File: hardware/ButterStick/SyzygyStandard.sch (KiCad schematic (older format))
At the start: 9 parts, among them J1 SYZYGY-STD, U2 DAC081C081CIMK, U7 TPS73101DBV

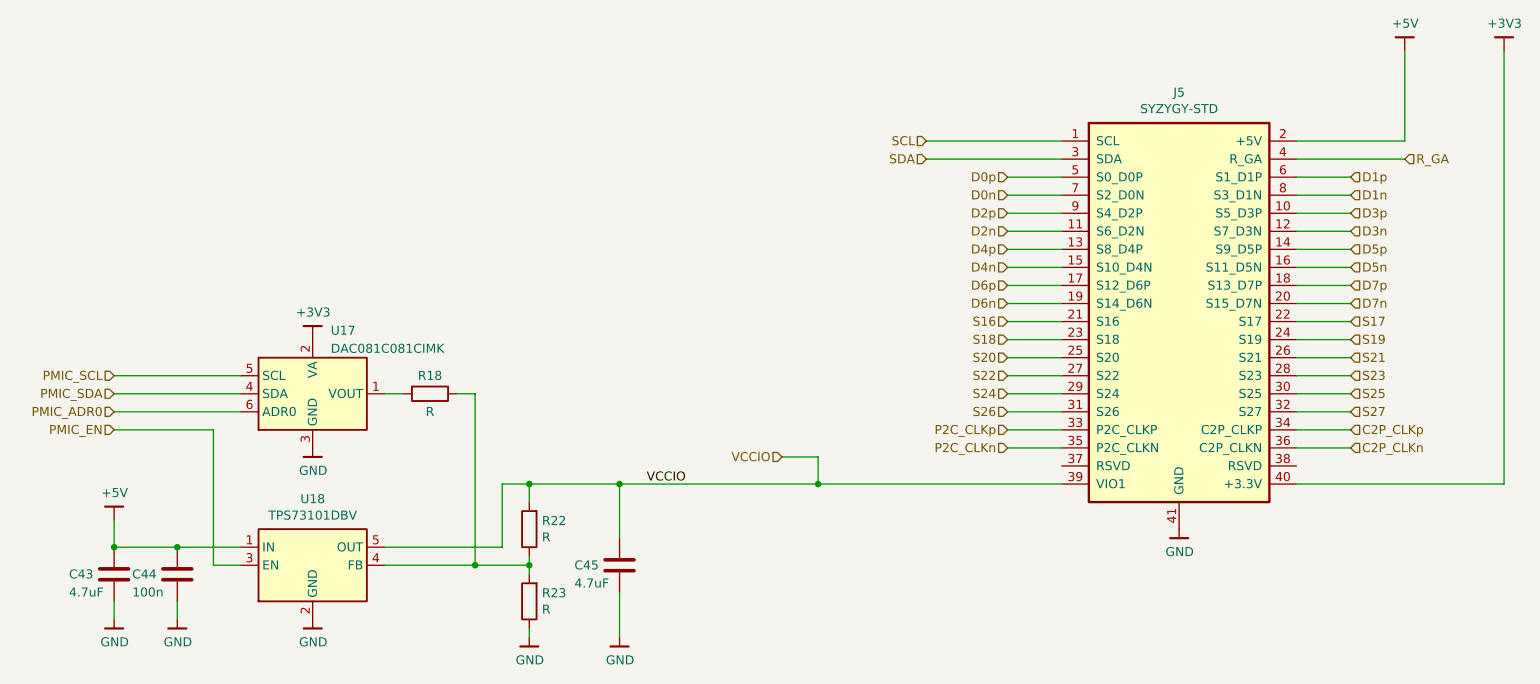
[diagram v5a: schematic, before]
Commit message: Finalised part values update BOM values to reflect. Swapped layers 4/5 due to stackup changes
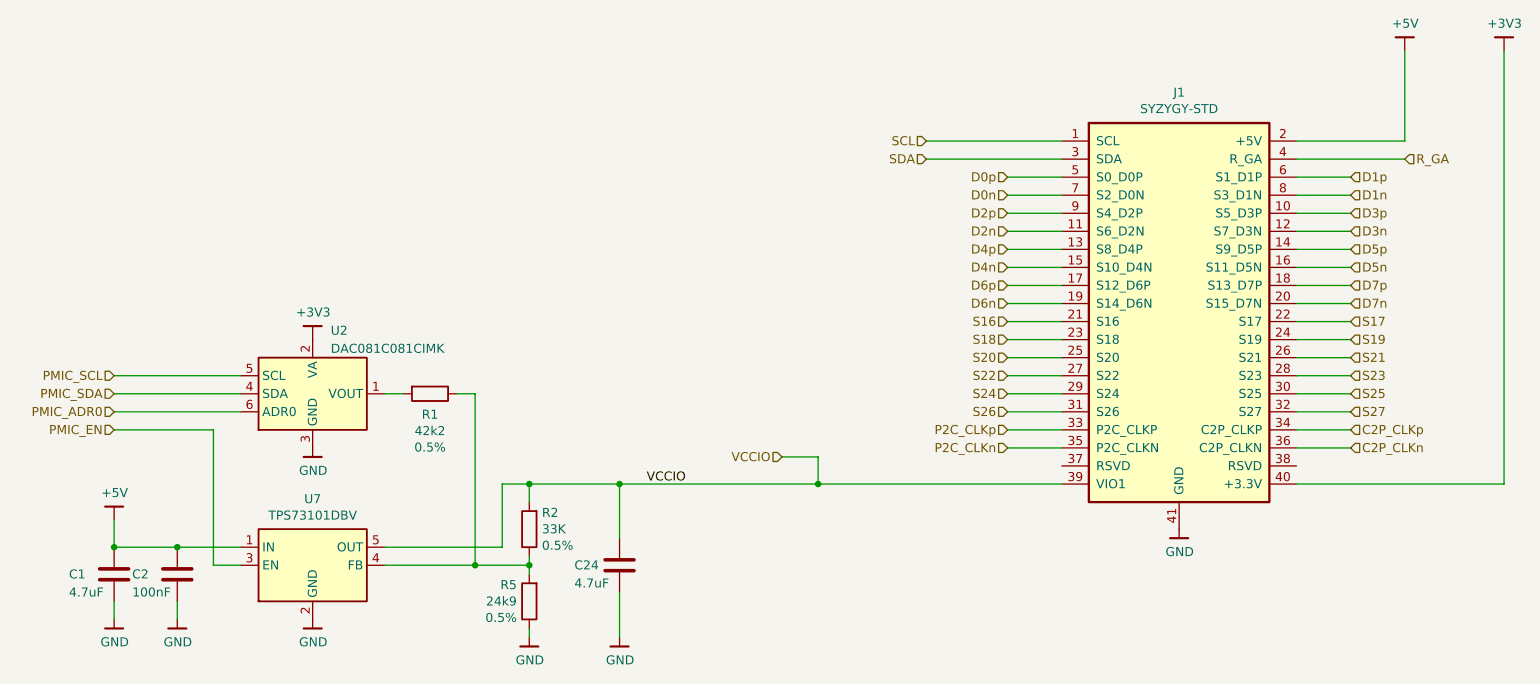
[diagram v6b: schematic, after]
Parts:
- C1, C24: Mfg (none) -> Samsung Electro-Mechanics; PN (none) -> CL10A475KP8NNNC
- C2: value 100n -> 100nF; Mfg (none) -> Samsung Electro-Mechanics; PN (none) -> CL05B104KP5NNNC
- J1: Mfg (none) -> Samtec Inc.; PN (none) -> QSE-020-01-F-D-A
- R1: value R -> 42k2; Mfg (none) -> Stackpole Electronics Inc; PN (none) -> RNCF0402DTE42K2; Tol (none) -> 0.5%
- R2: value R -> 33K; Mfg (none) -> Stackpole Electronics Inc; PN (none) -> RNCF0402DTE33K0; Tol (none) -> 0.5%
- R5: value R -> 24k9; Mfg (none) -> Stackpole Electronics Inc; PN (none) -> RNCF0402DTE24K9; Tol (none) -> 0.5%
- U2: Mfg (none) -> Texas Instruments; PN (none) -> DAC081C081CIMK/NOPB
- U7: Mfg (none) -> Texas Instruments; PN (none) -> TPS73101DBVR
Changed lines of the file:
@@
 EESchema Schematic File Version 4
 LIBS:ButterStick-cache
-EELAYER 26 0
+EELAYER 29 0
 EELAYER END
 $Descr A4 11693 8268
 encoding utf-8
-Sheet 8 13
-Title ""
-Date ""
-Rev ""
-Comp ""
+Sheet 6 13
+Title "ButterStick"
+Date "2019-03-19"
+Rev "r0_1"
+Comp "GsD"
 Comment1 ""
 Comment2 ""
@@
 AR Path="/5C80F19D/5C8A3B67/5C813052" Ref="J3"  Part="1"
 AR Path="/5C80F1A0/5C8EBB21/5C813052" Ref="J5"  Part="1"
-F 0 "J5" H 7850 4819 50  0000 C CNN
+F 0 "J1" H 7850 4819 50  0000 C CNN
 F 1 "SYZYGY-STD" H 7850 4728 50  0000 C CNN
 F 2 "gkl_conn:SYZYGY_standard_carrier" H 7850 4700 50  0001 C CNN
 F 3 "" H 7850 4700 50  0001 C CNN
+F 4 "Samtec Inc." H 0   0   50  0001 C CNN "Mfg"
+F 5 "QSE-020-01-F-D-A" H 0   0   50  0001 C CNN "PN"
 	1    7850 3700
 	1    0    0    -1
@@
 AR Path="/5C80F19D/5C8A3B67/5C939EEE" Ref="U16"  Part="1"
 AR Path="/5C80F1A0/5C8EBB21/5C939EEE" Ref="U18"  Part="1"
-F 0 "U18" H 3050 5567 50  0000 C CNN
+F 0 "U7" H 3050 5567 50  0000 C CNN
 F 1 "TPS73101DBV" H 3050 5476 50  0000 C CNN
 F 2 "Package_TO_SOT_SMD:SOT-23-5" H 3050 5525 50  0001 C CIN
 F 3 "http://www.ti.com/lit/ds/symlink/tps731.pdf" H 3050 5150 50  0001 C CNN
+F 4 "Texas Instruments" H 0   0   50  0001 C CNN "Mfg"
+F 5 "TPS73101DBVR" H 0   0   50  0001 C CNN "PN"
 	1    3050 5200
 	1    0    0    -1
@@
 AR Path="/5C80F19D/5C8A3B67/5C939EF5" Ref="U12"  Part="1"
 AR Path="/5C80F1A0/5C8EBB21/5C939EF5" Ref="U17"  Part="1"
-F 0 "U17" H 3150 4600 50  0000 L CNN
+F 0 "U2" H 3150 4600 50  0000 L CNN
 F 1 "DAC081C081CIMK" H 3150 4500 50  0000 L CNN
 F 2 "Package_TO_SOT_SMD:SOT-23-6" H 3700 4000 50  0001 C CNN
 F 3 "http://www.ti.com/lit/ds/symlink/dac081c081.pdf" H 3050 4250 50  0001 C CNN
+F 4 "Texas Instruments" H 0   0   50  0001 C CNN "Mfg"
+F 5 "DAC081C081CIMK/NOPB" H 0   0   50  0001 C CNN "PN"
 	1    3050 4250
 	1    0    0    -1
@@
 AR Path="/5C80F19D/5C8A3B67/5C9A2E64" Ref="#PWR0140"  Part="1"
 AR Path="/5C80F1A0/5C8EBB21/5C9A2E64" Ref="#PWR0183"  Part="1"
-F 0 "#PWR0183" H 3050 4300 50  0001 C CNN
+F 0 "#PWR0125" H 3050 4300 50  0001 C CNN
 F 1 "GND" H 3053 4424 50  0000 C CNN
 F 2 "" H 2950 4200 50  0001 C CNN
@@
 AR Path="/5C80F19D/5C8A3B67/5C939F02" Ref="#PWR0173"  Part="1"
 AR Path="/5C80F1A0/5C8EBB21/5C939F02" Ref="#PWR0184"  Part="1"
-F 0 "#PWR0184" H 3050 5250 50  0001 C CNN
+F 0 "#PWR0130" H 3050 5250 50  0001 C CNN
 F 1 "GND" H 3053 5374 50  0000 C CNN
 F 2 "" H 2950 5150 50  0001 C CNN
@@
 AR Path="/5C80F19D/5C8A3B67/5C9A2E66" Ref="#PWR0174"  Part="1"
 AR Path="/5C80F1A0/5C8EBB21/5C9A2E66" Ref="#PWR0185"  Part="1"
-F 0 "#PWR0185" H 3050 3800 50  0001 C CNN
+F 0 "#PWR0131" H 3050 3800 50  0001 C CNN
 F 1 "+3V3" H 3053 4101 50  0000 C CNN
 F 2 "" H 3050 3950 50  0001 C CNN
@@
 AR Path="/5C80F19D/5C8A3B67/5C939F0E" Ref="#PWR0175"  Part="1"
 AR Path="/5C80F1A0/5C8EBB21/5C939F0E" Ref="#PWR0186"  Part="1"
-F 0 "#PWR0186" H 1950 4800 50  0001 C CNN
+F 0 "#PWR0132" H 1950 4800 50  0001 C CNN
 F 1 "+5V" H 1953 5101 50  0000 C CNN
 F 2 "" H 1950 4950 50  0001 C CNN
@@
 AR Path="/5C80F19D/5C8A3B67/5C9A2E68" Ref="C38"  Part="1"
 AR Path="/5C80F1A0/5C8EBB21/5C9A2E68" Ref="C43"  Part="1"
-F 0 "C43" H 1700 5250 50  0000 L CNN
+F 0 "C1" H 1700 5250 50  0000 L CNN
 F 1 "4.7uF" H 1700 5150 50  0000 L CNN
 F 2 "pkl_dipol:C_0603" H 1988 5100 50  0001 C CNN
 F 3 "~" H 1950 5250 50  0001 C CNN
+F 4 "Samsung Electro-Mechanics" H 0   0   50  0001 C CNN "Mfg"
+F 5 "CL10A475KP8NNNC" H 0   0   50  0001 C CNN "PN"
 	1    1950 5250
 	1    0    0    -1
@@
 AR Path="/5C80F19D/5C8A3B67/5C939F1D" Ref="C39"  Part="1"
 AR Path="/5C80F1A0/5C8EBB21/5C939F1D" Ref="C44"  Part="1"
-F 0 "C44" H 2050 5250 50  0000 L CNN
-F 1 "100n" H 2050 5150 50  0000 L CNN
+F 0 "C2" H 2050 5250 50  0000 L CNN
+F 1 "100nF" H 2050 5150 50  0000 L CNN
 F 2 "pkl_dipol:C_0402" H 2338 5100 50  0001 C CNN
 F 3 "~" H 2300 5250 50  0001 C CNN
+F 4 "Samsung Electro-Mechanics" H 0   0   50  0001 C CNN "Mfg"
+F 5 "CL05B104KP5NNNC" H 0   0   50  0001 C CNN "PN"
 	1    2300 5250
 	1    0    0    -1
@@
 AR Path="/5C80F19D/5C8A3B67/5C9A2E6A" Ref="R6"  Part="1"
 AR Path="/5C80F1A0/5C8EBB21/5C9A2E6A" Ref="R18"  Part="1"
-F 0 "R18" V 3600 4250 50  0000 C CNN
-F 1 "R" V 3800 4250 50  0000 C CNN
+F 0 "R1" V 3815 4250 50  0000 C CNN
+F 1 "42k2" V 3906 4250 50  0000 C CNN
 F 2 "pkl_dipol:C_0402" V 3630 4250 50  0001 C CNN
 F 3 "~" H 3700 4250 50  0001 C CNN
+F 4 "RNCF0402DTE42K2" H 3700 4250 50  0001 C CNN "PN"
+F 5 "Stackpole Electronics Inc" H 3700 4250 50  0001 C CNN "Mfg"
+F 6 "0.5%" V 3997 4250 50  0000 C CNN "Tol"
 	1    3700 4250
 	0    1    1    0
-$EndComp
-$Comp
-L Device:R R?
-U 1 1 5C939F38
-P 4250 5000
-AR Path="/5BBD18EA/5C939F38" Ref="R?"  Part="1"
-AR Path="/5C80F19A/5C812FEF/5C939F38" Ref="R2"  Part="1"
-AR Path="/5C80F19D/5C8A3B67/5C939F38" Ref="R16"  Part="1"
-AR Path="/5C80F1A0/5C8EBB21/5C939F38" Ref="R22"  Part="1"
-F 0 "R22" H 4180 4954 50  0000 R CNN
-F 1 "R" H 4180 5045 50  0000 R CNN
-F 2 "pkl_dipol:C_0402" V 4180 5000 50  0001 C CNN
-F 3 "~" H 4250 5000 50  0001 C CNN
-	1    4250 5000
-	-1   0    0    1
 $EndComp
 $Comp
@@
 AR Path="/5C80F19D/5C8A3B67/5C939F3F" Ref="R17"  Part="1"
 AR Path="/5C80F1A0/5C8EBB21/5C939F3F" Ref="R23"  Part="1"
-F 0 "R23" H 4180 5354 50  0000 R CNN
-F 1 "R" H 4180 5445 50  0000 R CNN
+F 0 "R5" H 4319 5309 50  0000 L CNN
+F 1 "24k9" H 4319 5400 50  0000 L CNN
 F 2 "pkl_dipol:C_0402" V 4180 5400 50  0001 C CNN
 F 3 "~" H 4250 5400 50  0001 C CNN
+F 4 "RNCF0402DTE24K9" H 4250 5400 50  0001 C CNN "PN"
+F 5 "Stackpole Electronics Inc" H 4250 5400 50  0001 C CNN "Mfg"
+F 6 "0.5%" H 4319 5491 50  0000 L CNN "Tol"
 	1    4250 5400
 	-1   0    0    1
@@
 AR Path="/5C80F19D/5C8A3B67/5C939F46" Ref="C42"  Part="1"
 AR Path="/5C80F1A0/5C8EBB21/5C939F46" Ref="C45"  Part="1"
-F 0 "C45" H 4500 5200 50  0000 L CNN
+F 0 "C24" H 4500 5200 50  0000 L CNN
 F 1 "4.7uF" H 4500 5100 50  0000 L CNN
 F 2 "pkl_dipol:C_0603" H 4788 5050 50  0001 C CNN
 F 3 "~" H 4750 5200 50  0001 C CNN
+F 4 "Samsung Electro-Mechanics" H 0   0   50  0001 C CNN "Mfg"
+F 5 "CL10A475KP8NNNC" H 0   0   50  0001 C CNN "PN"
 	1    4750 5200
 	1    0    0    -1
@@
 AR Path="/5C80F19D/5C8A3B67/5C939F4E" Ref="#PWR0176"  Part="1"
 AR Path="/5C80F1A0/5C8EBB21/5C939F4E" Ref="#PWR0187"  Part="1"
-F 0 "#PWR0187" H 4250 5350 50  0001 C CNN
+F 0 "#PWR0133" H 4250 5350 50  0001 C CNN
 F 1 "GND" H 4253 5474 50  0000 C CNN
 F 2 "" H 4150 5250 50  0001 C CNN
@@
 AR Path="/5C80F19D/5C8A3B67/5C9A2E6F" Ref="#PWR0177"  Part="1"
 AR Path="/5C80F1A0/5C8EBB21/5C9A2E6F" Ref="#PWR0188"  Part="1"
-F 0 "#PWR0188" H 4750 5350 50  0001 C CNN
+F 0 "#PWR0134" H 4750 5350 50  0001 C CNN
 F 1 "GND" H 4753 5474 50  0000 C CNN
 F 2 "" H 4650 5250 50  0001 C CNN
@@
 AR Path="/5C80F19D/5C8A3B67/5C939F6F" Ref="#PWR0178"  Part="1"
 AR Path="/5C80F1A0/5C8EBB21/5C939F6F" Ref="#PWR0189"  Part="1"
-F 0 "#PWR0189" H 2300 5250 50  0001 C CNN
+F 0 "#PWR0135" H 2300 5250 50  0001 C CNN
 F 1 "GND" H 2303 5374 50  0000 C CNN
 F 2 "" H 2200 5150 50  0001 C CNN
@@
 AR Path="/5C80F19D/5C8A3B67/5C939F75" Ref="#PWR0179"  Part="1"
 AR Path="/5C80F1A0/5C8EBB21/5C939F75" Ref="#PWR0190"  Part="1"
-F 0 "#PWR0190" H 1950 5250 50  0001 C CNN
+F 0 "#PWR0137" H 1950 5250 50  0001 C CNN
 F 1 "GND" H 1953 5374 50  0000 C CNN
 F 2 "" H 1850 5150 50  0001 C CNN
@@
 AR Path="/5C80F19D/5C8A3B67/5C946418" Ref="#PWR0181"  Part="1"
 AR Path="/5C80F1A0/5C8EBB21/5C946418" Ref="#PWR0191"  Part="1"
-F 0 "#PWR0191" H 9100 2200 50  0001 C CNN
+F 0 "#PWR0138" H 9100 2200 50  0001 C CNN
 F 1 "+5V" H 9103 2501 50  0000 C CNN
 F 2 "" H 9100 2350 50  0001 C CNN
@@
 AR Path="/5C80F19D/5C8A3B67/5C946494" Ref="#PWR0182"  Part="1"
 AR Path="/5C80F1A0/5C8EBB21/5C946494" Ref="#PWR0211"  Part="1"
-F 0 "#PWR0211" H 9650 2200 50  0001 C CNN
+F 0 "#PWR0139" H 9650 2200 50  0001 C CNN
 F 1 "+3V3" H 9653 2501 50  0000 C CNN
 F 2 "" H 9650 2350 50  0001 C CNN
@@
 AR Path="/5C80F19D/5C8A3B67/5CED2F7B" Ref="#PWR0265"  Part="1"
 AR Path="/5C80F1A0/5C8EBB21/5CED2F7B" Ref="#PWR0266"  Part="1"
-F 0 "#PWR0266" H 7850 4750 50  0001 C CNN
+F 0 "#PWR0264" H 7850 4750 50  0001 C CNN
 F 1 "GND" H 7853 4874 50  0000 C CNN
 F 2 "" H 7750 4650 50  0001 C CNN
@@
 Wire Wire Line
 	1950 4450 2500 4450
+$Comp
+L Device:R R?
+U 1 1 5C939F38
+P 4250 5000
+AR Path="/5BBD18EA/5C939F38" Ref="R?"  Part="1"
+AR Path="/5C80F19A/5C812FEF/5C939F38" Ref="R2"  Part="1"
+AR Path="/5C80F19D/5C8A3B67/5C939F38" Ref="R16"  Part="1"
+AR Path="/5C80F1A0/5C8EBB21/5C939F38" Ref="R22"  Part="1"
+F 0 "R2" H 4180 4909 50  0000 R CNN
+F 1 "33K" H 4180 5000 50  0000 R CNN
+F 2 "pkl_dipol:C_0402" V 4180 5000 50  0001 C CNN
+F 3 "~" H 4250 5000 50  0001 C CNN
+F 4 "RNCF0402DTE33K0" H 4250 5000 50  0001 C CNN "PN"
+F 5 "Stackpole Electronics Inc" H 4250 5000 50  0001 C CNN "Mfg"
+F 6 "0.5%" H 4180 5091 50  0000 R CNN "Tol"
+	1    4250 5000
+	-1   0    0    1
+$EndComp
 $EndSCHEMATC
